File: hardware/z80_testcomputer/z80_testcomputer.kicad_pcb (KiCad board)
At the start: 2 copper layers, 95 x 100 mm, 13 parts, among them J1 Conn_02x15_Odd_Even, J2 Conn_02x15_Odd_Even, U1 Z84C000XPEG

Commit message: first bus connections
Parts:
- moved C1 0.26 mm to (124.5, 125.8)
- moved C2 0.26 mm to (124.5, 123.8)
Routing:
- net /VDD: track 16.2 -> 143.2 mm, vias 0 -> 1
- net /VSS: track 110.6 -> 233.2 mm
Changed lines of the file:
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@@
     (thickness 1.6)
     (drawings 10)
-    (tracks 32)
+    (tracks 44)
     (zones 0)
     (modules 13)
@@
   )
   (module SquantorRcl:C_0805+0603 (layer B.Cu)
-    (at 124.425 123.5 180)
+    (at 124.5 123.75 180)
     (descr "Capacitor SMD 0805 and 0603 pad sizes, reflow soldering, based on AVX dimensions")
     (tags "capacitor 0805 0603 mixed")
@@
   )
   (module SquantorRcl:C_0805+0603 (layer B.Cu)
-    (at 124.425 125.5 180)
+    (at 124.5 125.75 180)
     (descr "Capacitor SMD 0805 and 0603 pad sizes, reflow soldering, based on AVX dimensions")
     (tags "capacitor 0805 0603 mixed")
@@
   (gr_line (start 195 150) (end 105 150) (layer Edge.Cuts) (width 0.15))
   (gr_line (start 105 50) (end 195 50) (layer Edge.Cuts) (width 0.15))
+  (segment (start 191.77 97.79) (end 193.675 97.79) (width 1) (layer B.Cu) (net 1))
+  (segment (start 191.77 80.01) (end 193.675 80.01) (width 1) (layer B.Cu) (net 1))
+  (segment (start 193.675 97.79) (end 193.675 87.63) (width 1) (layer B.Cu) (net 1))
+  (segment (start 193.675 110.49) (end 193.675 102.87) (width 1) (layer B.Cu) (net 1))
+  (segment (start 191.77 102.87) (end 193.675 102.87) (width 1) (layer B.Cu) (net 1))
+  (segment (start 184.31 59.69) (end 193.04 59.69) (width 1) (layer B.Cu) (net 1))
+  (segment (start 179 65) (end 184.31 59.69) (width 1) (layer B.Cu) (net 1))
+  (segment (start 193.675 87.63) (end 193.675 80.01) (width 1) (layer B.Cu) (net 1))
   (segment (start 191.77 138.43) (end 193.04 138.43) (width 1) (layer B.Cu) (net 1))
+  (segment (start 193.675 120.65) (end 193.675 110.49) (width 1) (layer B.Cu) (net 1))
+  (segment (start 125.5 65) (end 179 65) (width 1) (layer B.Cu) (net 1))
+  (segment (start 193.675 60.325) (end 193.675 69.85) (width 1) (layer B.Cu) (net 1))
+  (segment (start 191.77 87.63) (end 193.675 87.63) (width 1) (layer B.Cu) (net 1))
+  (segment (start 193.675 128.27) (end 193.675 120.65) (width 1) (layer B.Cu) (net 1))
+  (segment (start 193.04 59.69) (end 193.675 60.325) (width 1) (layer B.Cu) (net 1))
+  (segment (start 191.77 120.65) (end 193.675 120.65) (width 1) (layer B.Cu) (net 1))
+  (segment (start 191.77 110.49) (end 193.675 110.49) (width 1) (layer B.Cu) (net 1))
   (segment (start 193.04 138.43) (end 193.675 137.795) (width 1) (layer B.Cu) (net 1))
-  (segment (start 193.675 60.325) (end 193.04 59.69) (width 1) (layer B.Cu) (net 1))
-  (segment (start 193.04 59.69) (end 187.325 59.69) (width 1) (layer B.Cu) (net 1))
+  (segment (start 191.77 128.27) (end 193.675 128.27) (width 1) (layer B.Cu) (net 1))
+  (segment (start 193.675 80.01) (end 193.675 69.85) (width 1) (layer B.Cu) (net 1))
   (segment (start 191.77 69.85) (end 193.675 69.85) (width 1) (layer B.Cu) (net 1))
-  (segment (start 193.675 69.85) (end 193.675 60.325) (width 1) (layer B.Cu) (net 1))
-  (segment (start 191.77 80.01) (end 193.675 80.01) (width 1) (layer B.Cu) (net 1))
-  (segment (start 193.675 80.01) (end 193.675 69.85) (width 1) (layer B.Cu) (net 1))
-  (segment (start 191.77 87.63) (end 193.675 87.63) (width 1) (layer B.Cu) (net 1))
-  (segment (start 193.675 87.63) (end 193.675 80.01) (width 1) (layer B.Cu) (net 1))
-  (segment (start 191.77 97.79) (end 193.675 97.79) (width 1) (layer B.Cu) (net 1))
-  (segment (start 193.675 97.79) (end 193.675 87.63) (width 1) (layer B.Cu) (net 1))
-  (segment (start 191.77 102.87) (end 193.675 102.87) (width 1) (layer B.Cu) (net 1))
   (segment (start 193.675 102.87) (end 193.675 97.79) (width 1) (layer B.Cu) (net 1))
-  (segment (start 191.77 110.49) (end 193.675 110.49) (width 1) (layer B.Cu) (net 1))
-  (segment (start 193.675 110.49) (end 193.675 102.87) (width 1) (layer B.Cu) (net 1))
-  (segment (start 191.77 128.27) (end 193.675 128.27) (width 1) (layer B.Cu) (net 1))
   (segment (start 193.675 137.795) (end 193.675 128.27) (width 1) (layer B.Cu) (net 1))
-  (segment (start 191.77 120.65) (end 193.675 120.65) (width 1) (layer B.Cu) (net 1))
-  (segment (start 193.675 128.27) (end 193.675 120.65) (width 1) (layer B.Cu) (net 1))
-  (segment (start 193.675 120.65) (end 193.675 110.49) (width 1) (layer B.Cu) (net 1))
-  (segment (start 125.35 125.5) (end 126.5 125.5) (width 1) (layer B.Cu) (net 1))
-  (segment (start 126.94 125.94) (end 132.24 125.94) (width 1) (layer B.Cu) (net 1))
-  (segment (start 126.5 125.5) (end 126.94 125.94) (width 1) (layer B.Cu) (net 1))
-  (segment (start 125.35 125.5) (end 125.35 123.5) (width 1) (layer B.Cu) (net 1))
+  (segment (start 132.24 125.94) (end 126.94 125.94) (width 1) (layer B.Cu) (net 1))
+  (segment (start 126.75 125.75) (end 125.425 125.75) (width 1) (layer B.Cu) (net 1))
+  (segment (start 126.94 125.94) (end 126.75 125.75) (width 1) (layer B.Cu) (net 1))
+  (segment (start 125.425 125.75) (end 125.425 123.75) (width 1) (layer B.Cu) (net 1))
+  (segment (start 125.425 123.75) (end 125.425 122.575) (width 1) (layer B.Cu) (net 1))
+  (segment (start 125.5 122.5) (end 125.5 65) (width 1) (layer B.Cu) (net 1))
+  (segment (start 125.425 122.575) (end 125.5 122.5) (width 1) (layer B.Cu) (net 1))
   (segment (start 189.23 62.23) (end 189.23 64.77) (width 1) (layer B.Cu) (net 2))
   (segment (start 189.23 64.77) (end 191.77 64.77) (width 1) (layer B.Cu) (net 2))
   (segment (start 189.23 62.23) (end 191.77 62.23) (width 1) (layer B.Cu) (net 2))
-  (segment (start 122.1 123.5) (end 123.5 123.5) (width 1) (layer B.Cu) (net 2))
-  (segment (start 117 123.4) (end 122 123.4) (width 1) (layer B.Cu) (net 2))
-  (segment (start 122 123.4) (end 122.1 123.5) (width 1) (layer B.Cu) (net 2))
-  (segment (start 123.5 125.5) (end 123.5 123.5) (width 1) (layer B.Cu) (net 2))
+  (segment (start 189.23 62.23) (end 178.77 62.23) (width 1) (layer F.Cu) (net 2))
+  (segment (start 178.77 62.23) (end 178 63) (width 1) (layer F.Cu) (net 2))
+  (segment (start 178 63) (end 123.5 63) (width 1) (layer F.Cu) (net 2))
+  (segment (start 117 123.4) (end 121.9 123.4) (width 1) (layer B.Cu) (net 2))
+  (segment (start 122.25 123.75) (end 123.575 123.75) (width 1) (layer B.Cu) (net 2))
+  (segment (start 121.9 123.4) (end 122.25 123.75) (width 1) (layer B.Cu) (net 2))
+  (segment (start 123.575 125.75) (end 123.575 123.75) (width 1) (layer B.Cu) (net 2))
+  (via (at 123.5 63) (size 0.75) (drill 0.6) (layers F.Cu B.Cu) (net 2))
+  (segment (start 123.575 123.75) (end 123.575 122.575) (width 1) (layer B.Cu) (net 2))
+  (segment (start 123.5 122.5) (end 123.5 63) (width 1) (layer B.Cu) (net 2))
+  (segment (start 123.575 122.575) (end 123.5 122.5) (width 1) (layer B.Cu) (net 2))
   (zone (net 0) (net_name "") (layers F&B.Cu) (hatch edge 0.508)
     (connect_pads (clearance 0.508))

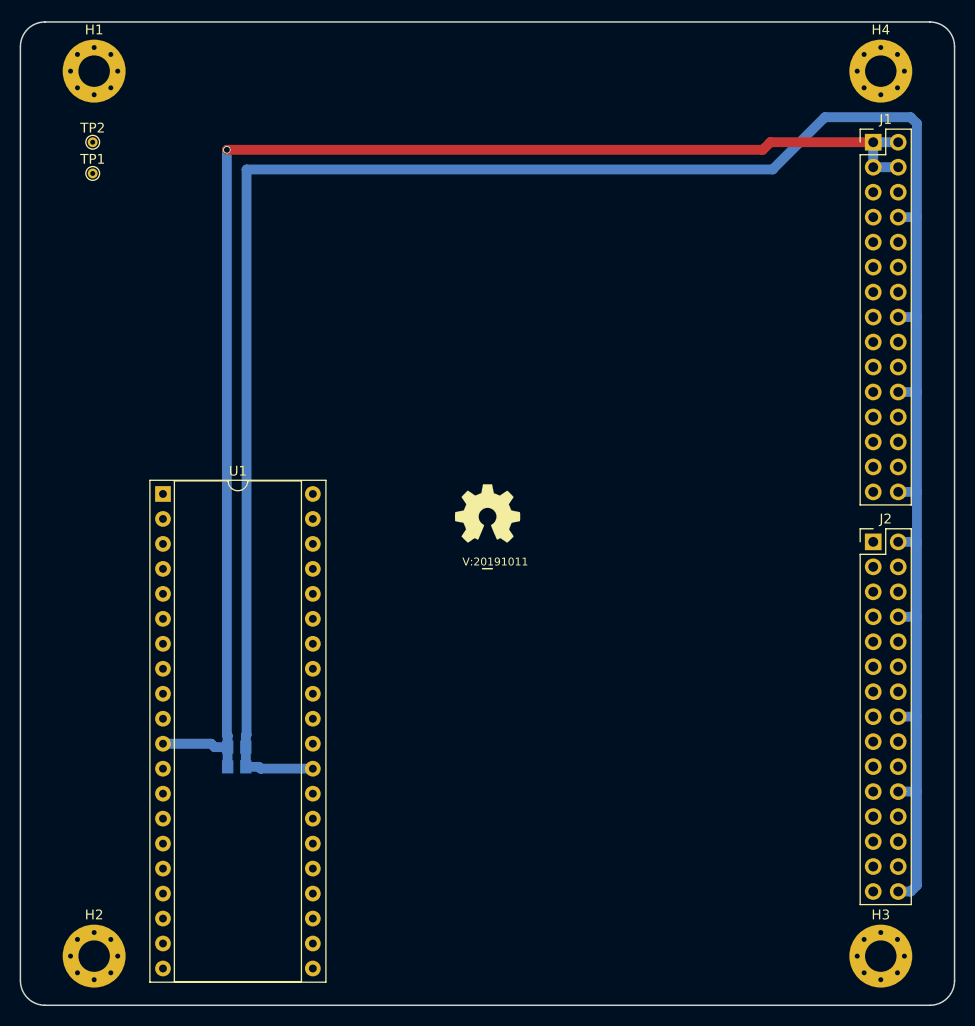
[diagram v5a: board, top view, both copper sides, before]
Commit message: some bus routing, lets add a RAM/ROM
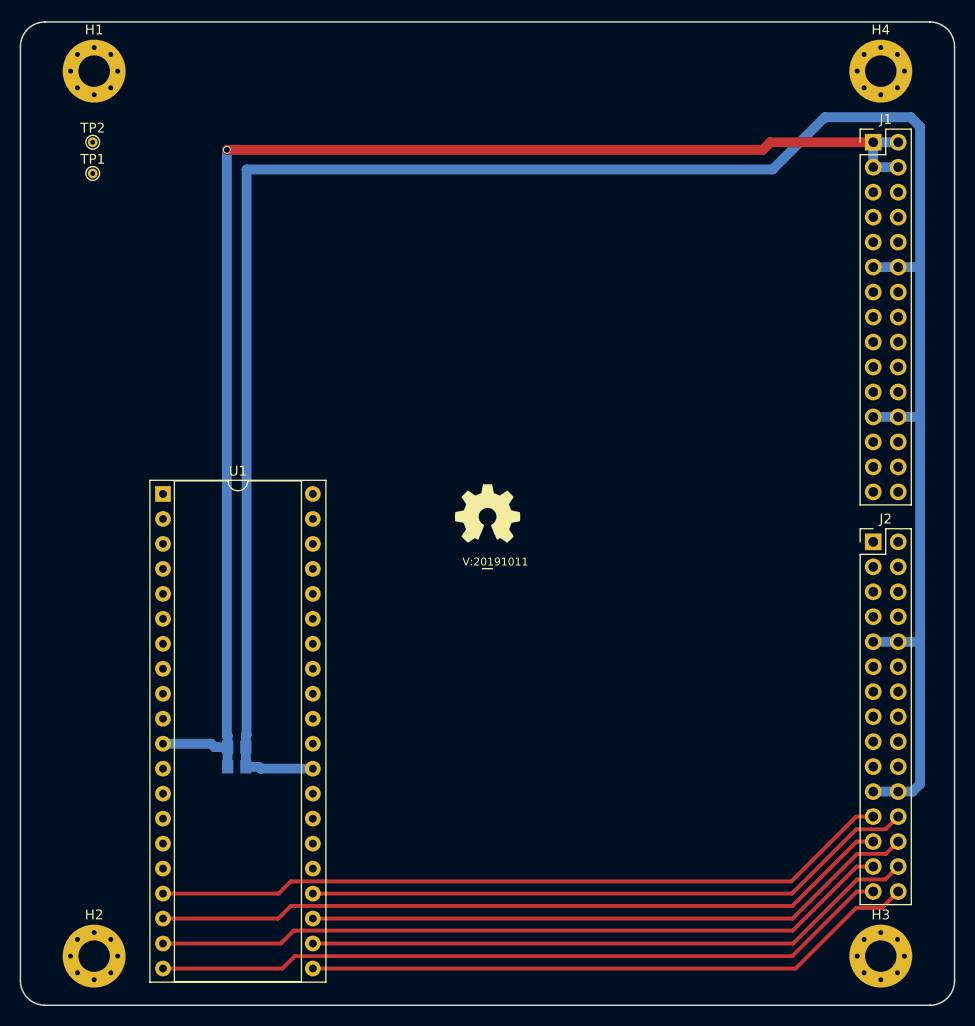
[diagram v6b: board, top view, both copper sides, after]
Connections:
- J1 pad 11: (no net) -> /VSS
- J1 pad 12: (no net) -> /VSS
- J1 pad 16: /VSS -> (no net)
- J1 pad 17: (no net) -> /A11
- J1 pad 18: (no net) -> /A10
- J1 pad 19: (no net) -> /A12
- J1 pad 20: (no net) -> /A9
- J1 pad 21: (no net) -> /A13
- J1 pad 22: /VSS -> /A8
- J1 pad 23: (no net) -> /VSS
- J1 pad 24: (no net) -> /VSS
- J1 pad 25: (no net) -> /A14
- J1 pad 26: (no net) -> /A7
- J1 pad 27: (no net) -> /A15
- J1 pad 28: (no net) -> /A6
- J1 pad 29: (no net) -> /MCLK
- J1 pad 30: /VSS -> /A5
- J1 pad 8: /VSS -> (no net)
- J2 pad 1: (no net) -> /D4
- J2 pad 10: (no net) -> /VSS
- J2 pad 11: (no net) -> /D2
- J2 pad 12: (no net) -> /A0
- J2 pad 13: (no net) -> /D7
- J2 pad 14: (no net) -> /!RFSH
- J2 pad 15: (no net) -> /D0
- J2 pad 16: /VSS -> /!M1
- J2 pad 17: (no net) -> /D1
- J2 pad 18: (no net) -> /!RESET
- J2 pad 19: (no net) -> /!INT
- J2 pad 2: /VSS -> /A4
- J2 pad 20: (no net) -> /!BUSREQ
- J2 pad 21: (no net) -> /VSS
- J2 pad 23: (no net) -> /!NMI
- J2 pad 24: (no net) -> /!WAIT
- J2 pad 25: (no net) -> /!HALT
- J2 pad 26: (no net) -> /!BUSACK
- J2 pad 27: (no net) -> /!MREQ
- J2 pad 28: (no net) -> /!WR
- J2 pad 29: (no net) -> /!IORQ
- J2 pad 3: (no net) -> /D3
- J2 pad 30: /VSS -> /!RD
- J2 pad 4: (no net) -> /A3
- J2 pad 5: (no net) -> /D5
- J2 pad 6: (no net) -> /A2
- J2 pad 7: (no net) -> /D6
- J2 pad 8: /VSS -> /A1
- J2 pad 9: (no net) -> /VSS
- U1 pad 1: (no net) -> /A11
- U1 pad 10: (no net) -> /D6
- U1 pad 12: (no net) -> /D2
- U1 pad 13: (no net) -> /D7
- U1 pad 14: (no net) -> /D0
- U1 pad 15: (no net) -> /D1
- U1 pad 16: (no net) -> /!INT
- U1 pad 17: (no net) -> /!NMI
- U1 pad 18: (no net) -> /!HALT
- U1 pad 19: (no net) -> /!MREQ
- U1 pad 2: (no net) -> /A12
- U1 pad 20: (no net) -> /!IORQ
- U1 pad 21: (no net) -> /!RD
- U1 pad 22: (no net) -> /!WR
- U1 pad 23: (no net) -> /!BUSACK
- U1 pad 24: (no net) -> /!WAIT
- U1 pad 25: (no net) -> /!BUSREQ
- U1 pad 26: (no net) -> /!RESET
- U1 pad 27: (no net) -> /!M1
- U1 pad 28: (no net) -> /!RFSH
- U1 pad 3: (no net) -> /A13
- U1 pad 30: (no net) -> /A0
- U1 pad 31: (no net) -> /A1
- U1 pad 32: (no net) -> /A2
- U1 pad 33: (no net) -> /A3
- U1 pad 34: (no net) -> /A4
- U1 pad 35: (no net) -> /A5
- U1 pad 36: (no net) -> /A6
- U1 pad 37: (no net) -> /A7
- U1 pad 38: (no net) -> /A8
- U1 pad 39: (no net) -> /A9
- U1 pad 4: (no net) -> /A14
- U1 pad 40: (no net) -> /A10
- U1 pad 5: (no net) -> /A15
- U1 pad 6: (no net) -> /MCLK
- U1 pad 7: (no net) -> /D4
- U1 pad 8: (no net) -> /D3
- U1 pad 9: (no net) -> /D5
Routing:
- net /!MREQ: track 0.00 -> 75.5 mm
- net /!HALT: track 0.00 -> 75.5 mm
- net /!IORQ: track 0.00 -> 75.5 mm
- net /!NMI: track 0.00 -> 75.5 mm
- net /!WR: track 0.00 -> 62.8 mm
- net /!BUSACK: track 0.00 -> 62.8 mm
- net /!WAIT: track 0.00 -> 62.8 mm
- net /!RD: track 0.00 -> 62.8 mm
- net /VSS: track 233.2 -> 225.1 mm
